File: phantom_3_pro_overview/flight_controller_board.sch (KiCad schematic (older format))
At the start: 0 parts

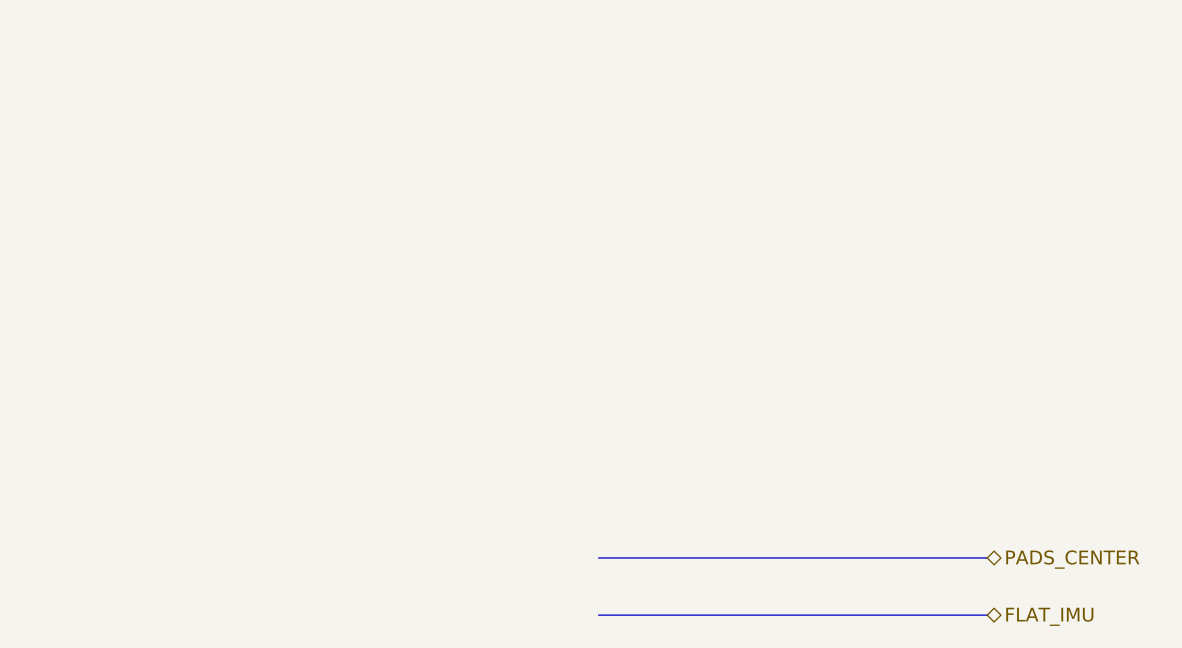
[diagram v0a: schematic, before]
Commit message: Overview: Conceptual schematics of some components.
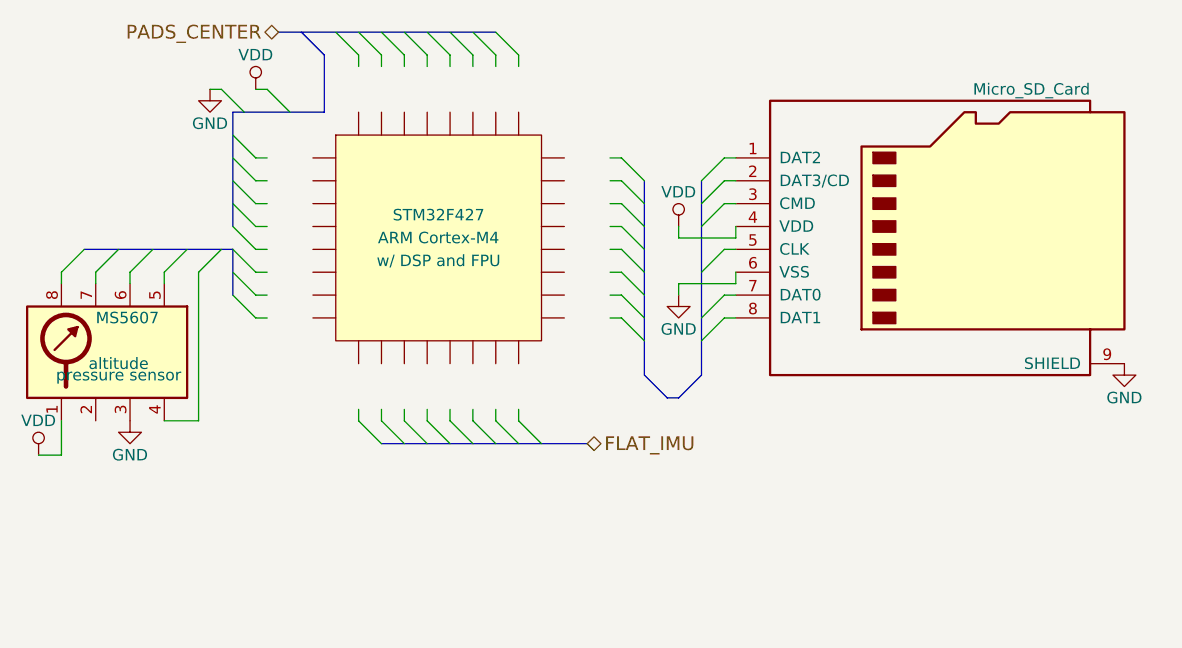
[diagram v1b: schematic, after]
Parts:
- added J?: Micro_SD_Card, symbol Micro_SD_Card
- added U?: STM32F427, ARM Cortex-M4, symbol IC_PQFP32
- added U?: MS5607, altitude, symbol MS5607
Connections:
- net labels added: GND, VDD
- wire segments 0 -> 54

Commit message: Overview: Added OFDM board.
Besides drawing the OFDM, components were updated.
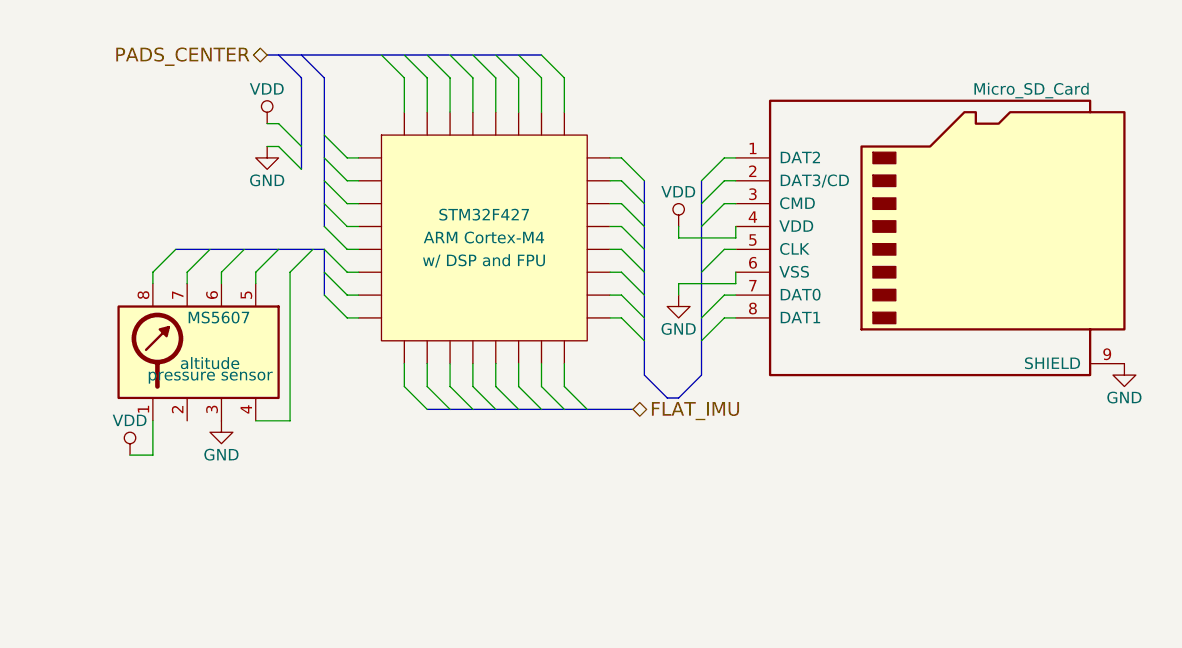
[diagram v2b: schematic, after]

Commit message: Overview: Upgraded to KiCAD 5.0.1.
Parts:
- J?: symbol Micro_SD_Card -> phantom_3_pro_overview-rescue:Micro_SD_Card
- U?: symbol IC_PQFP32 -> ic_dil_generic:IC_PQFP32
- U?: symbol MS5607 -> sensors:MS5607
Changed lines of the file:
@@
-EESchema Schematic File Version 2
-LIBS:power
-LIBS:device
-LIBS:transistors
-LIBS:conn
-LIBS:linear
-LIBS:regul
-LIBS:74xx
-LIBS:cmos4000
-LIBS:adc-dac
-LIBS:memory
-LIBS:xilinx
-LIBS:microcontrollers
-LIBS:dsp
-LIBS:microchip
-LIBS:analog_switches
-LIBS:motorola
-LIBS:texas
-LIBS:intel
-LIBS:audio
-LIBS:interface
-LIBS:digital-audio
-LIBS:philips
-LIBS:display
-LIBS:cypress
-LIBS:siliconi
-LIBS:opto
-LIBS:atmel
-LIBS:contrib
-LIBS:valves
-LIBS:motors
-LIBS:ic_dil_generic
-LIBS:sensors
-LIBS:u-blox
-LIBS:amplifiers
-LIBS:transistors-switches
-LIBS:transistors-power
-LIBS:sensors-v2
-LIBS:regul-v2
+EESchema Schematic File Version 4
 LIBS:phantom_3_pro_overview-cache
-EELAYER 25 0
+EELAYER 26 0
 EELAYER END
 $Descr User 6299 4370
@@
 FLAT_IMU
 $Comp
-L IC_PQFP32 U?
+L ic_dil_generic:IC_PQFP32 U?
 U 1 1 596E516F
 P 2700 1500
@@
 $EndComp
 $Comp
-L Micro_SD_Card J?
+L phantom_3_pro_overview-rescue:Micro_SD_Card J?
 U 1 1 596E5BE7
 P 4700 1450
@@
 $EndComp
 $Comp
-L GND #PWR?
+L power:GND #PWR?
 U 1 1 596E5C67
 P 5500 2050
@@
 	1900 700  2000 800
 $Comp
-L MS5607 U?
+L sensors:MS5607 U?
 U 1 1 596E72EC
 P 1500 2000
@@
 	1350 1550 1250 1650
 $Comp
-L GND #PWR?
+L power:GND #PWR?
 U 1 1 596E749A
 P 1750 1100
@@
 	1850 1650 1950 1550
 $Comp
-L GND #PWR?
+L power:GND #PWR?
 U 1 1 596E7704
 P 1550 2300
@@
 $EndComp
 $Comp
-L VDD #PWR?
+L power:VDD #PWR?
 U 1 1 596E777E
 P 1750 1000
@@
 $EndComp
 $Comp
-L VDD #PWR?
+L power:VDD #PWR?
 U 1 1 596E7792
 P 3550 1450
@@
 $EndComp
 $Comp
-L VDD #PWR?
+L power:VDD #PWR?
 U 1 1 596E77A6
 P 1150 2450
@@
 $EndComp
 $Comp
-L GND #PWR?
+L power:GND #PWR?
 U 1 1 596E7819
 P 3550 1750

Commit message: All: Finished updating to KiCad 5.0.1.
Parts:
- J?: symbol phantom_3_pro_overview-rescue:Micro_SD_Card -> Connector:Micro_SD_Card
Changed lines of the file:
@@
 $EndComp
 $Comp
-L phantom_3_pro_overview-rescue:Micro_SD_Card J?
+L Connector:Micro_SD_Card J?
 U 1 1 596E5BE7
 P 4700 1450
+AR Path="/596E5BE7" Ref="J?"  Part="1"
+AR Path="/596C09C9/596E5BE7" Ref="J?"  Part="1"
 F 0 "J?" H 4050 2050 50  0001 C CNN
 F 1 "Micro_SD_Card" H 5350 2050 50  0000 R CNN
@@
 	2100 1850 2150 1850
 Wire Bus Line
-	2450 2250 3350 2250
-Wire Bus Line
-	3650 2100 3650 1250
-Wire Bus Line
-	3400 1250 3400 2100
-Wire Bus Line
-	1750 700  2950 700
-Wire Bus Line
-	2000 800  2000 1450
-Wire Bus Line
 	3500 2200 3550 2200
 Wire Wire Line
@@
 Wire Wire Line
 	1750 1000 1800 1000
-Wire Bus Line
-	1350 1550 2000 1550
-Wire Bus Line
-	2000 1550 2000 1750
 Wire Wire Line
 	1850 2300 1850 1650
@@
 	1800 700  1900 800
 Wire Bus Line
+	2000 1550 2000 1750
+Wire Bus Line
 	1900 800  1900 1200
+Wire Bus Line
+	1350 1550 2000 1550
+Wire Bus Line
+	3650 1250 3650 2100
+Wire Bus Line
+	2000 800  2000 1450
+Wire Bus Line
+	1750 700  2950 700
+Wire Bus Line
+	2450 2250 3350 2250
+Wire Bus Line
+	3400 1250 3400 2100
 $EndSCHEMATC
